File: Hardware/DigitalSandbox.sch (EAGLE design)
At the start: 76 parts, among them Q1 MOSFET-PCHANNELSMD, Q2 MOSFET-NCHANNELBSS138, U1 ATMEGA328, U2 MCP9700, U3 TEMT6000, U4 MCP73831, U5 FT232RLSSOP, U6 V_REG_LDOSMD, U8 LMV358, U9 MIC9.7MM, X2 USB-SMD-NS, Y1 8MHz

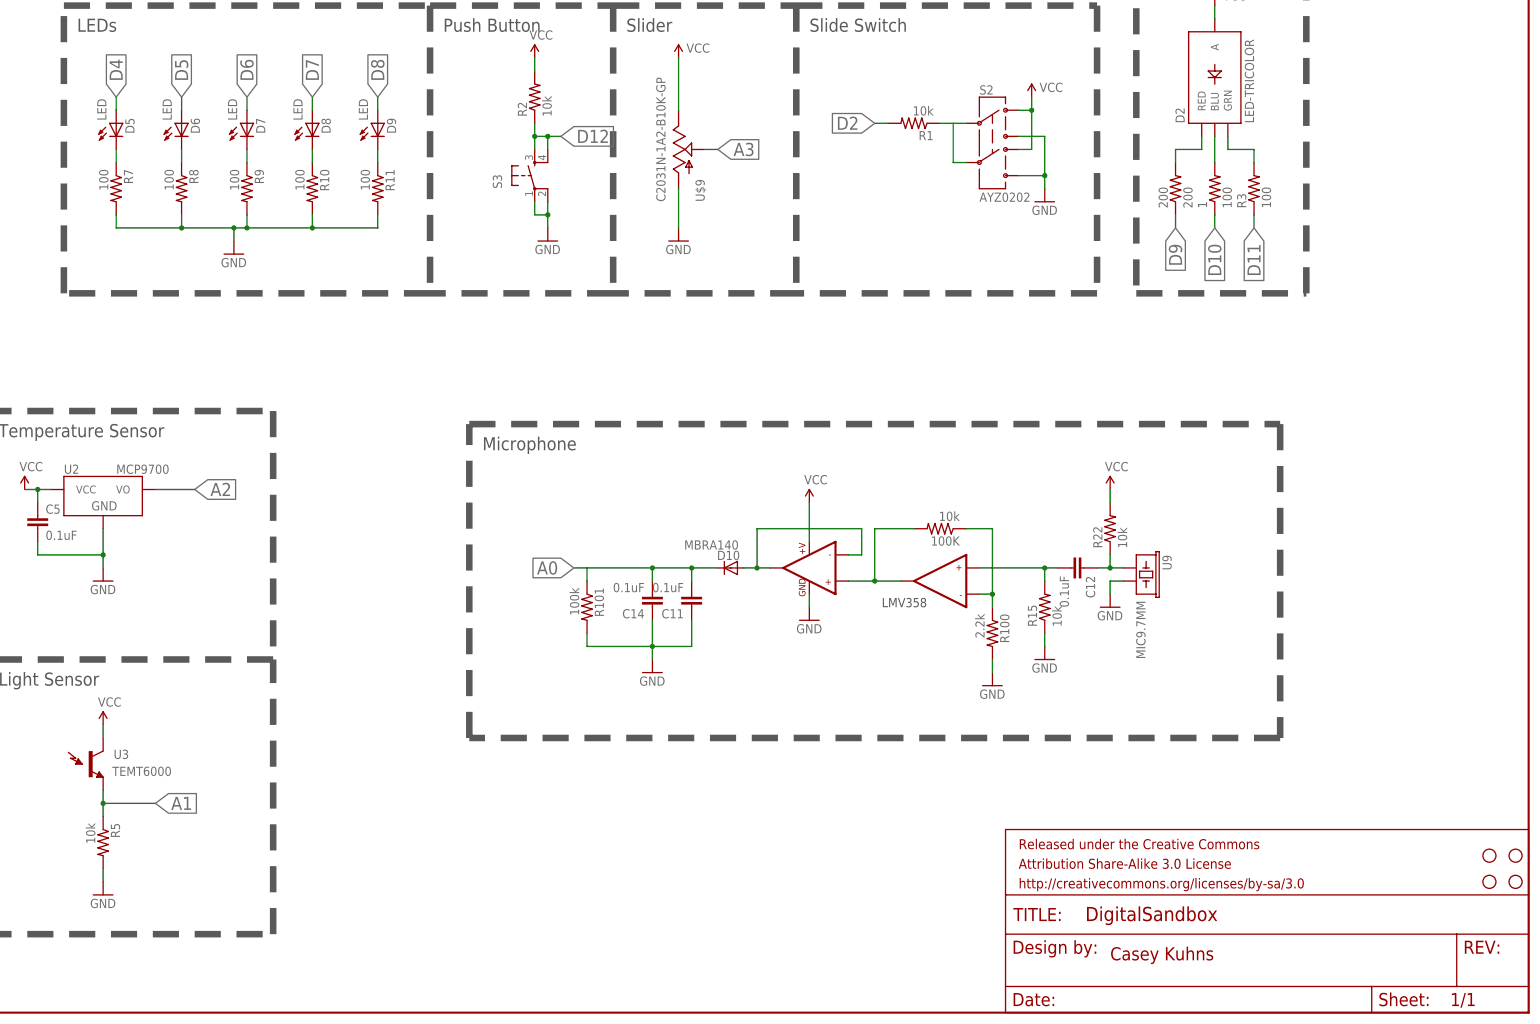
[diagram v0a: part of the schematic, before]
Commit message: Modified layout according to design review findings. Still working on silk.
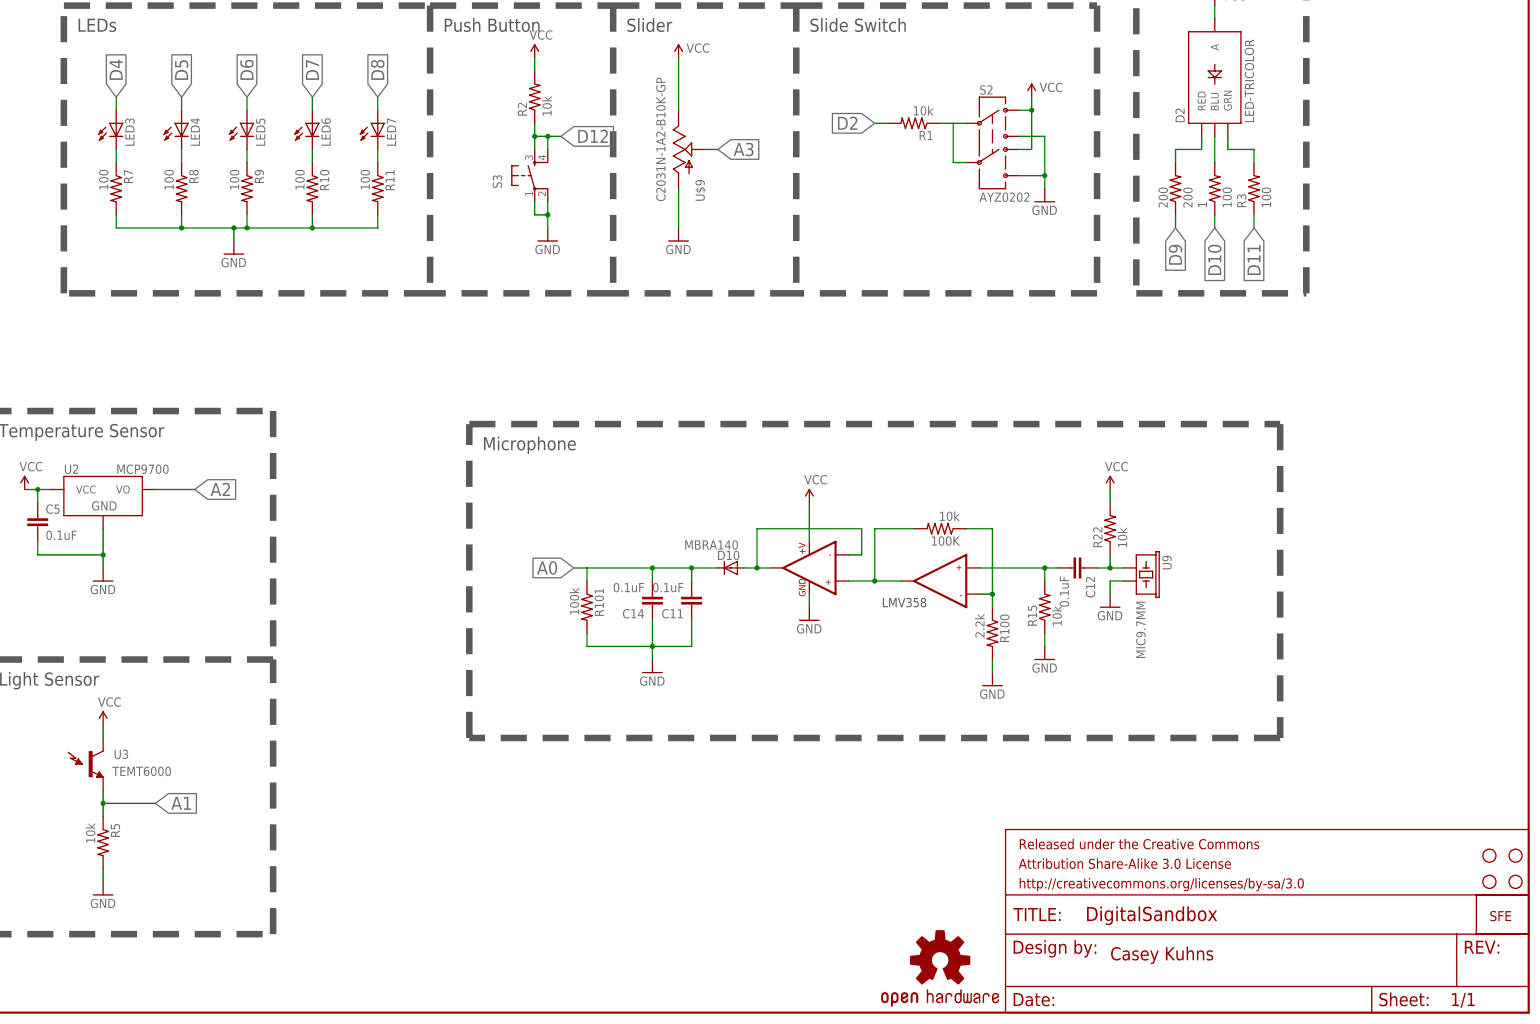
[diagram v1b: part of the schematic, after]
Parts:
- removed D5, D6, D7, D8, D9: LED, SparkFun:LED0603
- added LED3, LED4, LED5, LED6, LED7: (no value), SparkFun-LED:LED1206
- added LOGO1: OSHW-LOGOM, SparkFun-Aesthetics:OSHW-LOGOM
- added LOGO2: LOGO-SFENEW, SparkFun-Aesthetics:LOGO-SFENEW
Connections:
- net D4: now also LED3.A; no longer D5.A
- net D5: now also LED4.A; no longer D6.A
- net D6: now also LED5.A; no longer D7.A
- net D7: now also LED6.A; no longer D8.A
- net D8: now also LED7.A; no longer D9.A
- net N$11: now also LED6.C; no longer D8.C
- net N$13: now also LED7.C; no longer D9.C
- net N$18: now also LED3.C; no longer D5.C
- net N$21: now also LED4.C; no longer D6.C
- net N$9: now also LED5.C; no longer D7.C
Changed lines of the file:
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@@
 <part name="C1" library="SparkFun" deviceset="CAP" device="0603-CAP" value="0.1uF"/>
 <part name="C4" library="SparkFun" deviceset="CAP" device="0603-CAP" value="1.0uF"/>
-<part name="D5" library="SparkFun" deviceset="LED" device="0603" value="LED"/>
-<part name="D6" library="SparkFun" deviceset="LED" device="0603" value="LED"/>
-<part name="D7" library="SparkFun" deviceset="LED" device="0603" value="LED"/>
-<part name="D8" library="SparkFun" deviceset="LED" device="0603" value="LED"/>
-<part name="D9" library="SparkFun" deviceset="LED" device="0603" value="LED"/>
 <part name="GND8" library="SparkFun" deviceset="GND" device=""/>
 <part name="R1" library="SparkFun-Passives" deviceset="RESISTOR" device="0603-RES" value="10k"/>
@@
 <part name="C13" library="SparkFun" deviceset="CAP" device="0603-CAP" value="0.1uF"/>
 <part name="GND33" library="SparkFun" deviceset="GND" device=""/>
+<part name="LED3" library="SparkFun-LED" deviceset="LED" device="1206"/>
+<part name="LED4" library="SparkFun-LED" deviceset="LED" device="1206"/>
+<part name="LED5" library="SparkFun-LED" deviceset="LED" device="1206"/>
+<part name="LED6" library="SparkFun-LED" deviceset="LED" device="1206"/>
+<part name="LED7" library="SparkFun-LED" deviceset="LED" device="1206"/>
+<part name="LOGO2" library="SparkFun-Aesthetics" deviceset="LOGO-SFE" device="NEW"/>
+<part name="LOGO1" library="SparkFun-Aesthetics" deviceset="OSHW-LOGO" device="M"/>
 </parts>
 <sheets>
@@
 <instance part="C1" gate="G$1" x="5.08" y="-185.42" rot="R90"/>
 <instance part="C4" gate="G$1" x="48.26" y="-167.64"/>
-<instance part="D5" gate="G$1" x="134.62" y="-193.04" smashed="yes">
-<attribute name="NAME" x="138.176" y="-195.072" size="1.778" layer="95" rot="R90"/>
-<attribute name="VALUE" x="132.715" y="-192.532" size="1.778" layer="96" rot="R90"/>
-</instance>
-<instance part="D6" gate="G$1" x="147.32" y="-193.04" smashed="yes">
-<attribute name="NAME" x="150.876" y="-195.072" size="1.778" layer="95" rot="R90"/>
-<attribute name="VALUE" x="145.415" y="-192.532" size="1.778" layer="96" rot="R90"/>
-</instance>
-<instance part="D7" gate="G$1" x="160.02" y="-193.04" smashed="yes">
-<attribute name="NAME" x="163.576" y="-195.072" size="1.778" layer="95" rot="R90"/>
-<attribute name="VALUE" x="158.115" y="-192.532" size="1.778" layer="96" rot="R90"/>
-</instance>
-<instance part="D8" gate="G$1" x="172.72" y="-193.04" smashed="yes">
-<attribute name="NAME" x="176.276" y="-195.072" size="1.778" layer="95" rot="R90"/>
-<attribute name="VALUE" x="170.815" y="-192.532" size="1.778" layer="96" rot="R90"/>
-</instance>
-<instance part="D9" gate="G$1" x="185.42" y="-193.04" smashed="yes">
-<attribute name="NAME" x="188.976" y="-195.072" size="1.778" layer="95" rot="R90"/>
-<attribute name="VALUE" x="183.515" y="-192.532" size="1.778" layer="96" rot="R90"/>
-</instance>
 <instance part="GND8" gate="1" x="157.48" y="-218.44"/>
 <instance part="R1" gate="G$1" x="289.56" y="-193.04" rot="R180"/>
@@
 <instance part="C13" gate="G$1" x="381" y="-137.16"/>
 <instance part="GND33" gate="1" x="381" y="-142.24" rot="MR0"/>
+<instance part="LED3" gate="G$1" x="134.62" y="-193.04"/>
+<instance part="LED4" gate="G$1" x="147.32" y="-193.04"/>
+<instance part="LED5" gate="G$1" x="160.02" y="-193.04"/>
+<instance part="LED6" gate="G$1" x="172.72" y="-193.04"/>
+<instance part="LED7" gate="G$1" x="185.42" y="-193.04"/>
+<instance part="LOGO2" gate="G$1" x="401.32" y="-347.98"/>
+<instance part="LOGO1" gate="G$1" x="294.64" y="-355.6"/>
 </instances>
 <busses>
@@
 </segment>
 <segment>
-<pinref part="D6" gate="G$1" pin="A"/>
 <wire x1="147.32" y1="-190.5" x2="147.32" y2="-187.96" width="0.1524" layer="91"/>
 <label x="147.32" y="-187.96" size="2.54" layer="95" rot="R90" xref="yes"/>
+<pinref part="LED4" gate="G$1" pin="A"/>
 </segment>
 </net>
@@
 </segment>
 <segment>
-<pinref part="D7" gate="G$1" pin="A"/>
 <wire x1="160.02" y1="-190.5" x2="160.02" y2="-187.96" width="0.1524" layer="91"/>
 <label x="160.02" y="-187.96" size="2.54" layer="95" rot="R90" xref="yes"/>
+<pinref part="LED5" gate="G$1" pin="A"/>
 </segment>
 </net>
@@
 <pinref part="R7" gate="G$1" pin="1"/>
 <wire x1="134.62" y1="-200.66" x2="134.62" y2="-198.12" width="0.1524" layer="91"/>
-<pinref part="D5" gate="G$1" pin="C"/>
+<pinref part="LED3" gate="G$1" pin="C"/>
 </segment>
 </net>
@@
 <pinref part="R8" gate="G$1" pin="1"/>
 <wire x1="147.32" y1="-200.66" x2="147.32" y2="-198.12" width="0.1524" layer="91"/>
-<pinref part="D6" gate="G$1" pin="C"/>
+<pinref part="LED4" gate="G$1" pin="C"/>
 </segment>
 </net>
@@
 </segment>
 <segment>
-<pinref part="D5" gate="G$1" pin="A"/>
 <wire x1="134.62" y1="-190.5" x2="134.62" y2="-187.96" width="0.1524" layer="91"/>
 <label x="134.62" y="-187.96" size="2.54" layer="95" rot="R90" xref="yes"/>
+<pinref part="LED3" gate="G$1" pin="A"/>
 </segment>
 </net>
@@
 </segment>
 <segment>
-<pinref part="D9" gate="G$1" pin="A"/>
 <wire x1="185.42" y1="-190.5" x2="185.42" y2="-187.96" width="0.1524" layer="91"/>
 <label x="185.42" y="-187.96" size="2.54" layer="95" rot="R90" xref="yes"/>
+<pinref part="LED7" gate="G$1" pin="A"/>
 </segment>
 </net>
@@
 </segment>
 <segment>
-<pinref part="D8" gate="G$1" pin="A"/>
 <wire x1="172.72" y1="-190.5" x2="172.72" y2="-187.96" width="0.1524" layer="91"/>
 <label x="172.72" y="-187.96" size="2.54" layer="95" rot="R90" xref="yes"/>
+<pinref part="LED6" gate="G$1" pin="A"/>
 </segment>
 </net>
@@
 <segment>
 <pinref part="R9" gate="G$1" pin="1"/>
-<pinref part="D7" gate="G$1" pin="C"/>
 <wire x1="160.02" y1="-200.66" x2="160.02" y2="-198.12" width="0.1524" layer="91"/>
+<pinref part="LED5" gate="G$1" pin="C"/>
 </segment>
 </net>
@@
 <segment>
 <pinref part="R10" gate="G$1" pin="1"/>
-<pinref part="D8" gate="G$1" pin="C"/>
 <wire x1="172.72" y1="-200.66" x2="172.72" y2="-198.12" width="0.1524" layer="91"/>
+<pinref part="LED6" gate="G$1" pin="C"/>
 </segment>
 </net>
@@
 <segment>
 <pinref part="R11" gate="G$1" pin="1"/>
-<pinref part="D9" gate="G$1" pin="C"/>
 <wire x1="185.42" y1="-200.66" x2="185.42" y2="-198.12" width="0.1524" layer="91"/>
-</segment>
-</net>
+<pinref part="LED7" gate="G$1" pin="C"/>
+</segment>
+</net>

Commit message: Added silk and moved some components
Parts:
- removed D10: MBRA140, SparkFun:DIODESMA
- removed LOGO1: OSHW-LOGOM, SparkFun-Aesthetics:OSHW-LOGOM
- removed LOGO2: LOGO-SFENEW, SparkFun-Aesthetics:LOGO-SFENEW
- removed R100: 2.2k, SparkFun-Passives:RESISTOR0603-RES
- removed R101: 100k, SparkFun-Passives:RESISTOR0603-RES
- removed R22: 10k, SparkFun-Passives:RESISTOR0603-RES
- removed U$9: C2031N-1A2-B10K-GP, C2031N-1A2-B10K-GP:C2031N-1A2-B10K-GP
- added D3: LED-TRICOLOR, SparkFun:LED-TRICOLOR
- added R19: 2.2k, SparkFun-Passives:RESISTOR0603-RES
- added R20, R21: 10k, SparkFun-Passives:RESISTOR0603-RES
- added U7: V_REG_LDOSMD, SparkFun-PowerIC:V_REG_LDOSMD
- C2: value 47uF -> 4.7uF; device SparkFun:CAP_POL3528 -> SparkFun-Passives:CAP0603-CAP
- C3: value 0.1uF -> 47uF; device SparkFun:CAP0402-CAP -> SparkFun:CAP_POL3528
- C5: value 0.1uF -> 4.7uF; device SparkFun:CAP0603-CAP -> SparkFun-Passives:CAP0603-CAP
- C6: value 4.7uF -> 0.1uF; device SparkFun-Passives:CAP0603-CAP -> SparkFun:CAP0603-CAP
- C7: value 4.7uF -> 0.1uF; device SparkFun-Passives:CAP0603-CAP -> SparkFun:CAP0402-CAP
- D1: value Status -> Yellow
- D2: value LED-TRICOLOR -> Status; device SparkFun:LED-TRICOLOR -> SparkFun:LED0603
- D4: value Yellow -> MBRA140; device SparkFun:LED0603 -> SparkFun:DIODESMA
- LED1: value Red -> (none); device SparkFun:LED0603 -> SparkFun-LED:LED1206
- LED2: value Green -> (none); device SparkFun:LED0603 -> SparkFun-LED:LED1206
- LED6: value (none) -> Red; device SparkFun-LED:LED1206 -> SparkFun:LED0603
- LED7: value (none) -> Green; device SparkFun-LED:LED1206 -> SparkFun:LED0603
- Q1: value MOSFET-PCHANNELSMD -> MOSFET-N; device SparkFun-DiscreteSemi:MOSFET-PCHANNELSMD -> SparkFun-DiscreteSemi:MOSFET-NCHANNELBSS138
- Q2: value MOSFET-NCHANNELBSS138 -> MOSFET-P; device SparkFun-DiscreteSemi:MOSFET-NCHANNELBSS138 -> SparkFun-DiscreteSemi:MOSFET-PCHANNELSMD
- R1: value 10k -> 330
- R11: value 100 -> 1k
- R13: value 330 -> 1k
- R14, R15: value 10k -> 1k
- R16: value 1k -> 100
- R17: value 1k -> 100k
- R18: value 1k -> 10k
- R3: value 100 -> 10k
- R4: value 1k -> 330
- R6: value 330 -> 100
- S1: value On/Off -> Reset; device SparkFun:AYZ0202 -> SparkFun:SWITCH-MOMENTARY-2SMD
- S2: value AYZ0202 -> On/Off
- S3: value (none) -> AYZ0202; device SparkFun:TAC_SWITCHSMD -> SparkFun:AYZ0202
- S4: value Reset -> (none); device SparkFun:SWITCH-MOMENTARY-2SMD -> SparkFun:TAC_SWITCHSMD
- U1: value ATMEGA328 -> MCP73831; device SparkFun:ATMEGA168 -> SparkFun:MCP73831
- U2: value MCP9700 -> ATMEGA328; device SparkFun:MCP9700SMD -> SparkFun:ATMEGA168
- U3: value TEMT6000 -> MCP9700; device SparkFun:TEMT6000 -> SparkFun:MCP9700SMD
- U4: value MCP73831 -> FT232RLSSOP; device SparkFun:MCP73831 -> SparkFun:FT232RLSSOP
- U5: value FT232RLSSOP -> C2031N-1A2-B10K-GP; device SparkFun:FT232RLSSOP -> C2031N-1A2-B10K-GP:C2031N-1A2-B10K-GP
- U6: value V_REG_LDOSMD -> TEMT6000; device SparkFun-PowerIC:V_REG_LDOSMD -> SparkFun:TEMT6000
- renumbered X2 to X1
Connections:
- net 3.3V: now also U4.3V3OUT; no longer U5.3V3OUT
- net 5V: now also C2.1, C7.1, D1.A, R11.2, R13.2, S2.1, S2.4, U1.VIN, U4.VCC, U4.VCCIO; no longer C3.1, C6.1, D4.A, R17.2, R18.2, S1.1, S1.4, U4.VIN, U5.VCC, U5.VCCIO
- net A0: now also C12.2, C13.2, D4.C, R17.1, U2.PC0(ADC0); no longer C11.2, C14.2, D10.C, R101.1, U1.PC0(ADC0)
- net A1: now also R12.1, U2.PC1(ADC1), U6.E1; no longer R5.1, U1.PC1(ADC1), U3.E1
- net A2: now also U2.PC2(ADC2), U3.VO; no longer U1.PC2(ADC2), U2.VO
- net A3: now also U2.PC3(ADC3), U5.S; no longer U$9.S, U1.PC3(ADC3)
- net A4: now also U2.PC4(ADC4/SDA); no longer U1.PC4(ADC4/SDA)
- net A5: now also U2.PC5(ADC5/SCL); no longer U1.PC5(ADC5/SCL)
- net BLU: now also D3.BLU; no longer D2.BLU
- net CTS: now also U4.CTS; no longer U5.CTS
- net D10: now also U2.PB2(SS/OC1B); no longer U1.PB2(SS/OC1B)
- net D11: now also R16.1, U2.PB3(MOSI/OC2); no longer R3.1, U1.PB3(MOSI/OC2)
- net D12: now also R18.1, S4.3, S4.4, U2.PB4(MISO); no longer R2.1, S3.3, S3.4, U1.PB4(MISO)
- net D13: now also R4.2, U2.PB5(SCK); no longer R13.2, U1.PB5(SCK)
- net D2: now also R5.2, U2.PD2(INT0); no longer R1.2, U1.PD2(INT0)
- net D3: now also R14.2, U2.PD3(INT1); no longer R4.2, U1.PD3(INT1)
- net D4: now also LED1.A, U2.PD4(XCK/T0); no longer LED3.A, U1.PD4(XCK/T0)
- net D5: now also LED2.A, U2.PD5(T1); no longer LED4.A, U1.PD5(T1)
- net D6: now also LED3.A, U2.PD6(AIN0); no longer LED5.A, U1.PD6(AIN0)
- net D7: now also LED4.A, U2.PD7(AIN1); no longer LED6.A, U1.PD7(AIN1)
- net D8: now also LED5.A, U2.PB0(ICP); no longer LED7.A, U1.PB0(ICP)
- net D9: now also U2.PB1(OC1A); no longer U1.PB1(OC1A)
- net DTR: now also U4.DTR; no longer U5.DTR
- net GND: now also C11.2, C12.1, C13.1, C2.2, C3.-, D2.C, Q1.S, R12.2, R17.2, R19.2, R20.1, R3.1, R6.2, S1.2, S3.3, S3.6, S4.1, U1.VSS, U2.AGND, U2.GND@1, U2.GND@2, U3.GND, U4.AGND, U4.GND18, U4.GND21, U4.GND7, U4.TEST, U5.A, U7.GND; no longer C11.1, C13.2, C14.1, C2.-, C3.2, D1.C, Q2.S, R100.2, R101.2, R11.2, R14.1, R15.1, R5.2, S2.3, S2.6, S3.1, S3.2, U$9.A, U1.AGND, U1.GND@1, U1.GND@2, U2.GND, U4.VSS, U5.AGND, U5.GND18, U5.GND21, U5.GND7, U5.TEST, U6.GND
- net GRN: now also D3.GRN, R16.2; no longer D2.GRN, R3.2
- net N$1: now also U2.PB6(XTAL1/TOSC1); no longer U1.PB6(XTAL1/TOSC1)
- net N$10: now also Q1.G, R14.1; no longer Q2.G, R4.1
- net N$11: now also LED4.C, R9.1; no longer LED6.C, R10.1
- net N$12: now also C11.1, U7.OUT; no longer C13.1, U6.OUT
- net N$13: now also LED5.C, R10.1; no longer LED7.C, R11.1
- net N$15: now also R5.1, S3.2, S3.5; no longer R1.1, S2.2, S2.5
- net N$17: now also C14.1, R21.1; no longer C12.1, R22.1
- net N$18: now also LED1.C, R6.1; no longer LED3.C, R7.1
- net N$2: now also D2.A, R4.1; no longer D1.A, R13.1
- net N$20: now also C14.2, R20.2; no longer C12.2, R15.2
- net N$21: now also LED2.C, R7.1; no longer LED4.C, R8.1
- net N$23: now also R19.1; no longer R100.1
- net N$24: now also D4.A; no longer D10.A
- net N$3: now also U2.PB7(XTAL2/TOSC2); no longer U1.PB7(XTAL2/TOSC2)
- net N$33: now also D1.C, R1.1; no longer D4.C, R6.1
- net N$4: now also Q1.D, Q2.G, R15.2; no longer Q1.G, Q2.D, R16.2
- net N$5: now also LED6.A, R11.1; no longer LED1.A, R17.1
- net N$6: now also LED7.A, R13.1; no longer LED2.A, R18.1
- net N$7: now also U7.EN, U7.IN; no longer U6.EN, U6.IN
- net N$8: now also Q2.D; no longer Q1.D
- net N$9: now also LED3.C, R8.1; no longer LED5.C, R9.1
- net PROG: now also R3.2, U1.PROG; no longer R14.2, U4.PROG
- net RED: now also D3.RED; no longer D2.RED
- net RST: now also R2.1, S1.1, U2.PC6(/RESET); no longer R12.1, S4.1, U1.PC6(/RESET)
- net RXI: now also U2.PD0(RXD), U4.RXD; no longer U1.PD0(RXD), U5.RXD
- net RXLED: now also LED7.C, U4.RXLED; no longer LED2.C, U5.RXLED
- net STAT: now also R1.2, U1.STAT; no longer R6.2, U4.STAT
- net TXLED: now also LED6.C, U4.TXLED; no longer LED1.C, U5.TXLED
- net TXO: now also U2.PD1(TXD), U4.TXD; no longer U1.PD1(TXD), U5.TXD
- net USB_D+: now also U4.USBDP; no longer U5.USBDP
- net USB_D-: now also U4.USBDM; no longer U5.USBDM
- net VBATT: now also C5.1, S2.3, S2.6, U1.VBAT; no longer C7.1, S1.3, S1.6, U4.VBAT
- net VCC: now also C3.+, C6.1, D3.A, Q2.S, R15.1, R18.2, R21.2, S2.2, S2.5, S3.1, S3.4, U2.AREF, U2.AVCC, U2.VCC@1, U2.VCC@2, U3.VCC, U5.E, U6.C1; no longer C2.+, C5.1, D2.A, Q1.S, R12.2, R16.1, R22.2, S1.2, S1.5, S2.1, S2.4, U$9.E, U1.AREF, U1.AVCC, U1.VCC@1, U1.VCC@2, U2.VCC, U3.C1
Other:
- note added: "0 - 1"
- note added: "Expansion Port 3.3v"
- note added: "v01"
- note removed: "I2C Port 3.3v"
- moved on the sheet: 1, 100K, 200, C11, C12, C13, C14, C5, C6, C7, C8, D1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
